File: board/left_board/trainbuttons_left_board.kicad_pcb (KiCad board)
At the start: 4 copper layers, 182 x 73 mm, 45 parts, among them J101 USB_C_Receptacle_USB2.0_16P, J102 HDMI_A, J401 UART, J801 DBG, SW201 SW_Push, SW202 SW_Push, SW203 SW_Push, SW204 SW_Push, SW205 SW_Push, SW206 SW_Push, SW207 SW_Push, SW208 SW_Push, SW209 SW_Push, SW210 SW_Push, SW211 SW_Push, SW212 SW_Push, SW213 SW_Push, SW801 RST, U401 STM32G0B0CETx, U501 LM317AEMP, Y601 48MHz

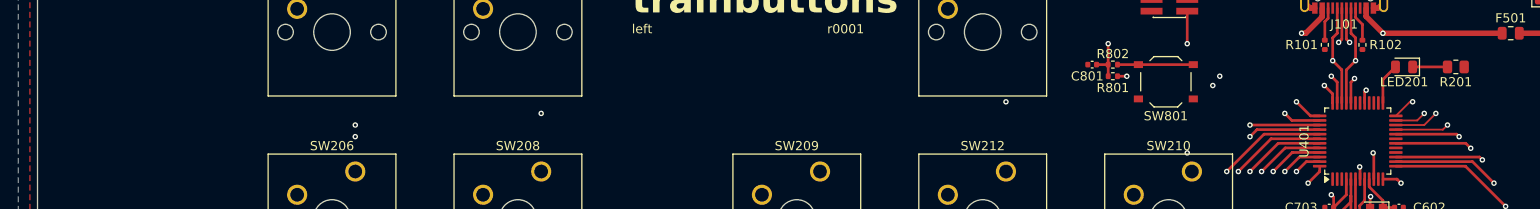
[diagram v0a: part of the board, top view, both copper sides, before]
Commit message: add support for pedal
the pedal is mostly envisioned as a secondary dead man's switch input, but
to enable flexible usage, it is wired up to the µC's ADC and supplies
12-bit values for the X axis

things will be set up to cooperate with a Brother-compatible sewing machine
pedal because that's what I have lying around -- those that connect using a
3.5mm TS phone connector, nothing even close to mains voltage
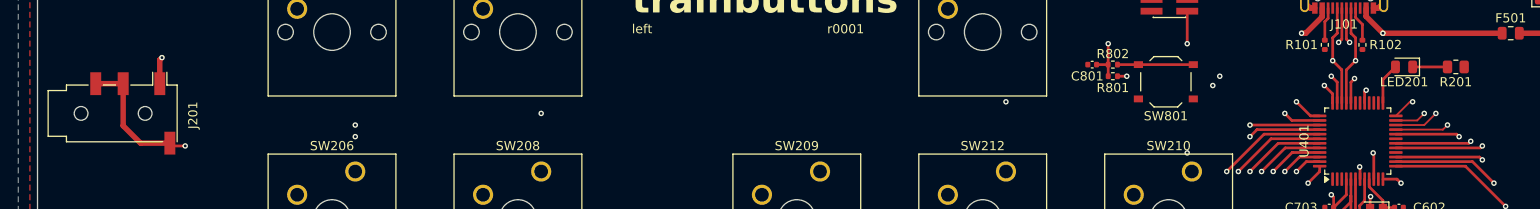
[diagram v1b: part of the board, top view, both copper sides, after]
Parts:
- added J201: AudioJack2, Connector_Audio:Jack_3.5mm_PJ320D_Horizontal, F.Cu at (39.6, 55.9)
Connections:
- U401 pad 17: unconnected-(U401-PA6-Pad17) -> /Left Buttons/PEDAL_ANA
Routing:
- net /Left Buttons/PEDAL_ANA: track 0.00 -> 166.8 mm, vias 0 -> 2
- net /Left Buttons/GND: track 8.16 -> 11.1 mm, vias 2 -> 3
- net /MCU/BRAKE_SCHG: track 39.9 -> 40.5 mm

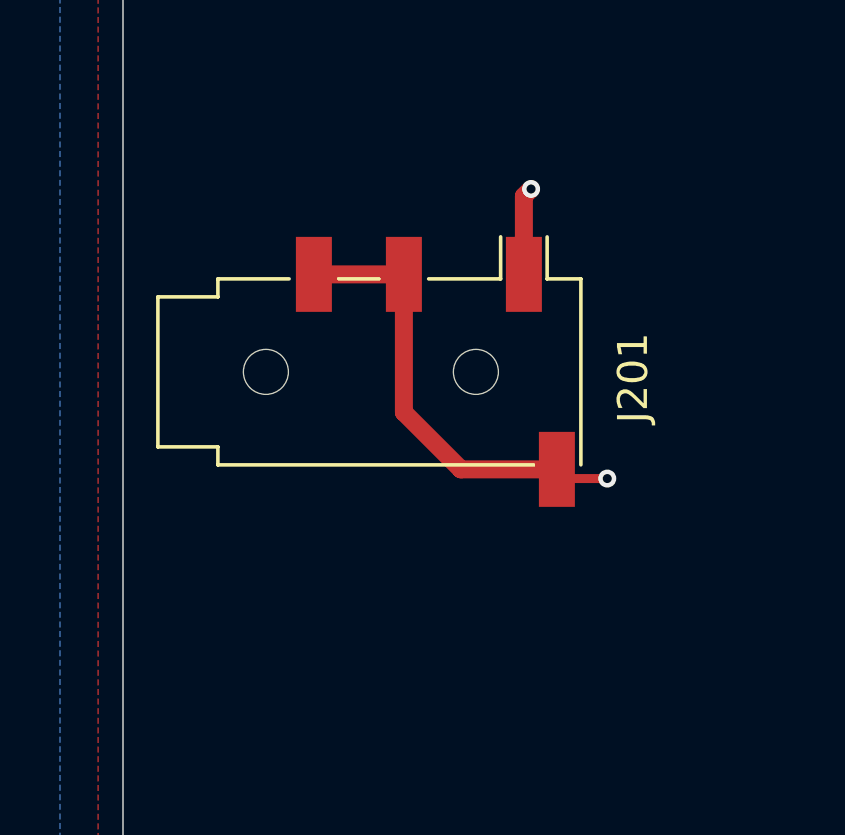
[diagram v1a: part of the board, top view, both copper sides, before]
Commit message: left board: pullup resistor for pedal
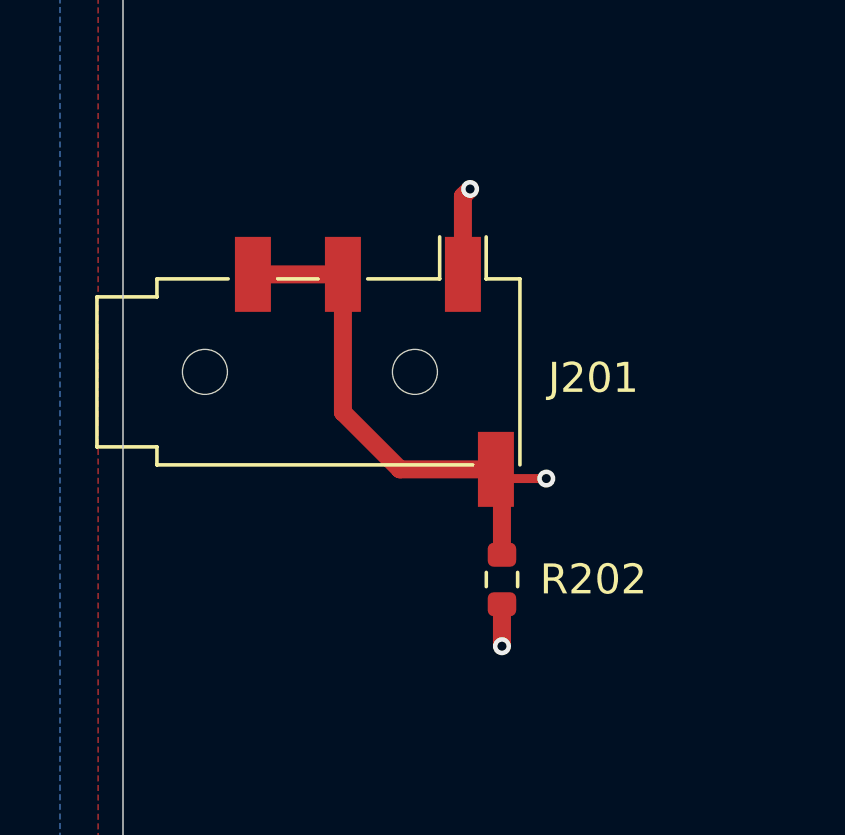
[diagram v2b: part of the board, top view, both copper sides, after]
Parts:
- added R202: 470kΩ, Resistor_SMD:R_0603_1608Metric, F.Cu at (42.7, 62.8)
- moved J201 2.03 mm to (37.5, 55.9)
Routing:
- net /Left Buttons/PEDAL_ANA: track 166.8 -> 171.0 mm
- net /Left Buttons/+3.3V: track 46.7 -> 48.1 mm, vias 8 -> 9
